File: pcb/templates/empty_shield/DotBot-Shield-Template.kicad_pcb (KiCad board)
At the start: 4 copper layers, 29 x 27 mm, 23 parts, among them J1 Conn_01x04, J2 Conn_01x10, J3 Conn_01x10, Q1 NX6008NBKWX, Q2 NX6008NBKWX, Q3 NX6008NBKWX, U1 ISM330DHCXTR, U2 TS4231, U4 LIS3MDL

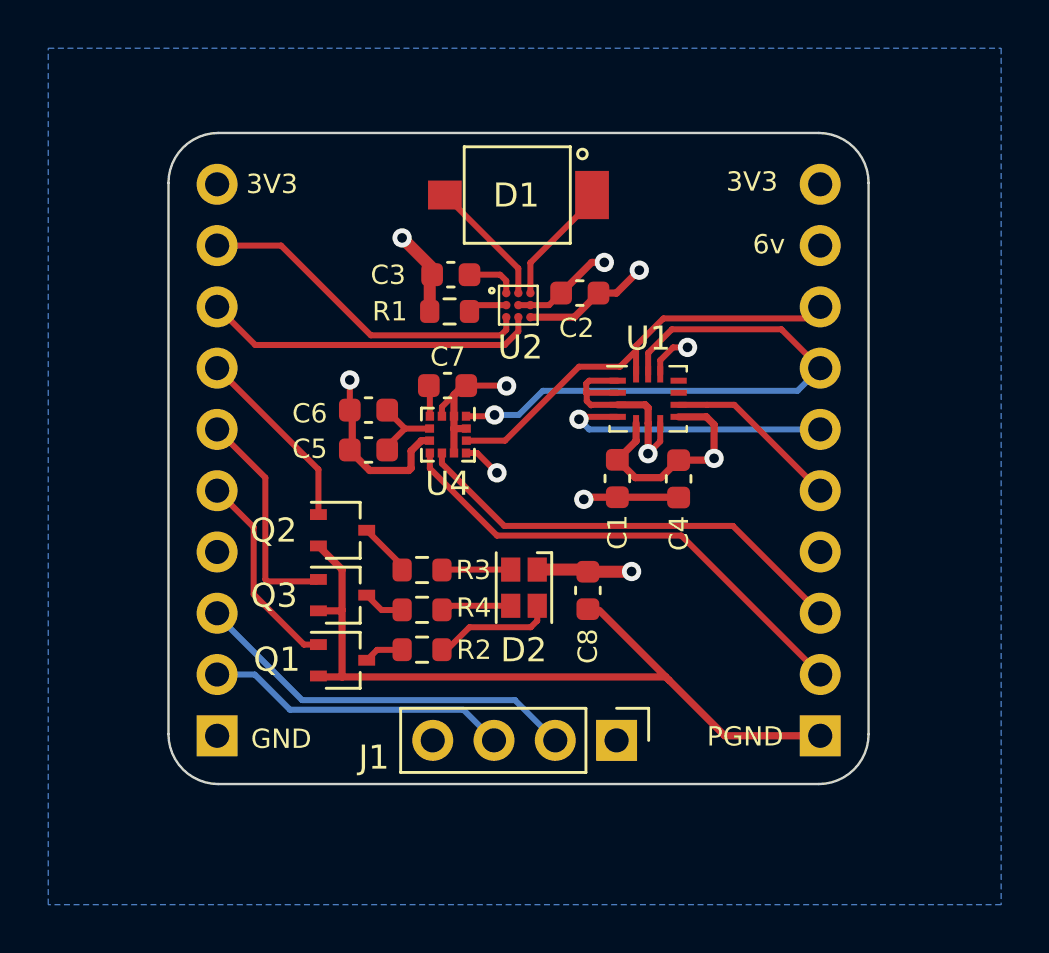
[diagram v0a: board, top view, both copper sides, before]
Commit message: #12 Remove unneeded components from the PCB
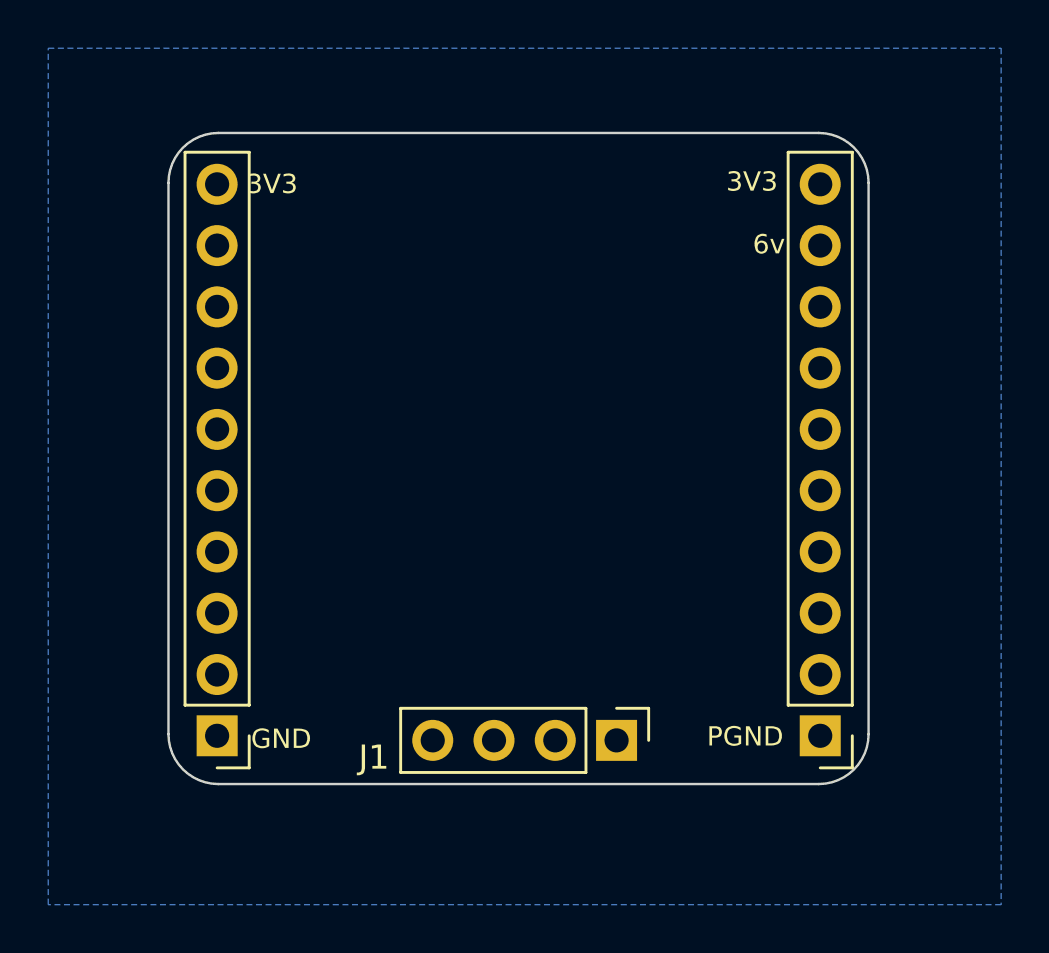
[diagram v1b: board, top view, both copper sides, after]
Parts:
- removed C1, C2, C4, C5, C7, C8: 100nF, Capacitor_SMD:C_0603_1608Metric
- removed C3, C6: 1uF, Capacitor_SMD:C_0603_1608Metric
- removed D1: BPW34S, DotBot:BPW34
- removed D2: CLMVC-FKA, LED_SMD:LED_Cree-PLCC4_2x2mm_CW
- removed Q1, Q2, Q3: NX6008NBKWX, Package_TO_SOT_SMD:SOT-323_SC-70
- removed R1: 15k, Resistor_SMD:R_0603_1608Metric
- removed R2: 1k, Resistor_SMD:R_0603_1608Metric
- removed R3, R4: 750, Resistor_SMD:R_0603_1608Metric
- removed U1: ISM330DHCXTR, Package_LGA:Bosch_LGA-14_3x2.5mm_P0.5mm
- removed U2: TS4231, DotBot:TS4231
- removed U4: LIS3MDL, Package_LGA:LGA-12_2x2mm_P0.5mm
- J1: value Conn_01x04 -> Bottom Header
- J2: value Conn_01x10 -> Left Header; moved to F.Cu
- J3: value Conn_01x10 -> Right Header; moved to F.Cu
- turned J2 to 180 degrees
- turned J3 to 180 degrees
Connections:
- J1 pad 2: EXT_2 -> unconnected-(J1-Pin_2-Pad2)
- J1 pad 3: EXT_1 -> unconnected-(J1-Pin_3-Pad3)
- J2 pad 2: EXT_1 -> unconnected-(J2-Pin_2-Pad2)
- J2 pad 3: EXT_2 -> unconnected-(J2-Pin_3-Pad3)
- J2 pad 5: LED_R -> unconnected-(J2-Pin_5-Pad5)
- J2 pad 6: LED_B -> unconnected-(J2-Pin_6-Pad6)
- J2 pad 7: LED_G -> unconnected-(J2-Pin_7-Pad7)
- J2 pad 8: LH2_E -> unconnected-(J2-Pin_8-Pad8)
- J2 pad 9: LH2_D -> unconnected-(J2-Pin_9-Pad9)
- J3 pad 2: INT -> unconnected-(J3-Pin_2-Pad2)
- J3 pad 3: DRDY -> unconnected-(J3-Pin_3-Pad3)
- J3 pad 5: INT2 -> unconnected-(J3-Pin_5-Pad5)
- J3 pad 6: INT1 -> unconnected-(J3-Pin_6-Pad6)
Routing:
- net GND: track 60.5 -> 0.00 mm, vias 5 -> 0
- net +3V3: track 25.7 -> 0.00 mm, vias 5 -> 0
- net SCL: track 24.6 -> 0.00 mm, vias 1 -> 0
- net +6V: track 23.4 -> 0.00 mm, vias 1 -> 0
- net INT: track 20.4 -> 0.00 mm
- net DRDY: track 18.7 -> 0.00 mm
- net SDA: track 18.1 -> 0.00 mm
- net EXT_2: track 16.2 -> 0.00 mm
- net LH2_D: track 14.1 -> 0.00 mm
- net LH2_E: track 14.0 -> 0.00 mm
- net EXT_1: track 12.6 -> 0.00 mm
- net INT1: track 11.8 -> 0.00 mm, vias 1 -> 0
- net LED_B: track 9.31 -> 0.00 mm
- net LED_R: track 8.47 -> 0.00 mm
- net LED_G: track 7.81 -> 0.00 mm
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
